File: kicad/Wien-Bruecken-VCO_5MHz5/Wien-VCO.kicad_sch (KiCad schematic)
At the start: 26 parts, among them J1 J113, U1 ${SIM.NAME}, U2 ${SIM.NAME}

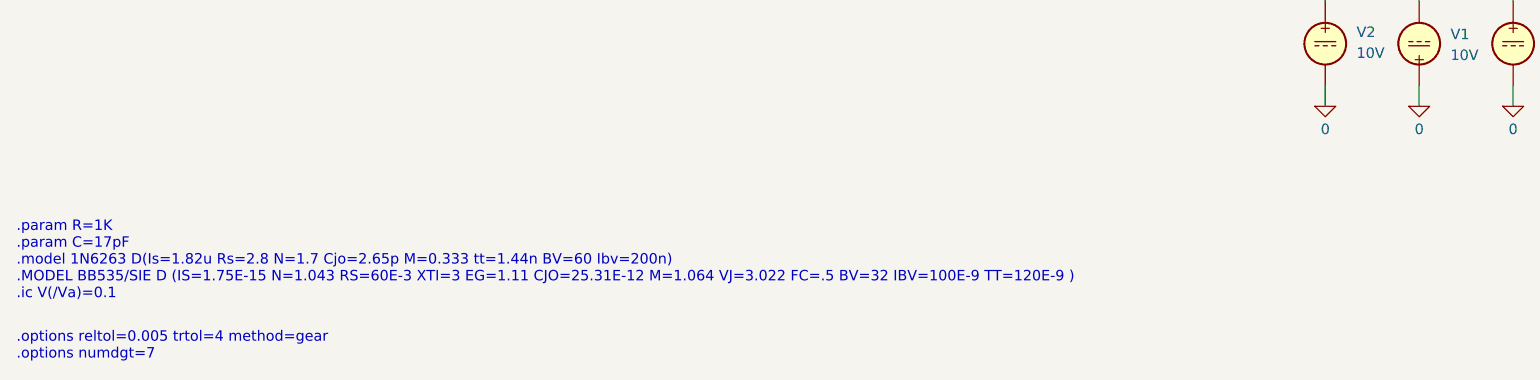
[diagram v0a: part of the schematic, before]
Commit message: sim Ordner angepasst
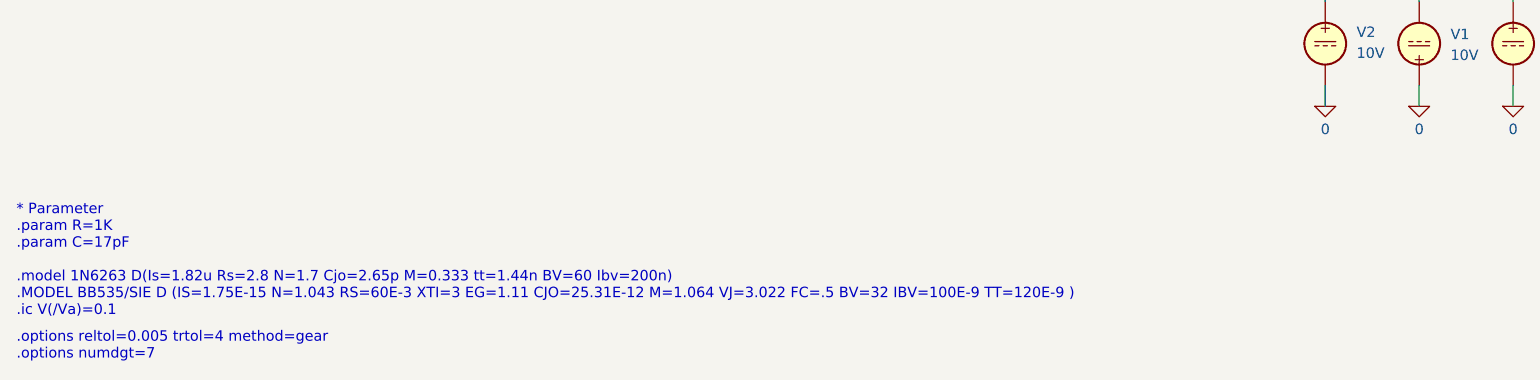
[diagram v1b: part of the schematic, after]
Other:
- note added: "* Parameter .param R=1K .param C=17pF .model 1N6263 D(Is=1.82u Rs=2.8 N=1.7 Cjo=2.65p M=0.333 tt=1.44n BV=60 Ibv=200n) .MODEL BB535/SIE D (IS=1.75E-15 N=1.043 RS=60E-3 XTI=3 EG=1.11 CJO=25.31E-12 M=1.064 VJ=3.022 FC=.5 BV=32 IBV=100E-9 TT=120E-9 ) .ic V(/Va)=0.1"
- note removed: ".param R=1K .param C=17pF .model 1N6263 D(Is=1.82u Rs=2.8 N=1.7 Cjo=2.65p M=0.333 tt=1.44n BV=60 Ibv=200n) .MODEL BB535/SIE D (IS=1.75E-15 N=1.043 RS=60E-3 XTI=3 EG=1.11 CJO=25.31E-12 M=1.064 VJ=3.022 FC=.5 BV=32 IBV=100E-9 TT=120E-9 ) .ic V(/Va)=0.1"
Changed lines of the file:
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@@
 	(generator_version "10.0")
 	(paper "A4")
-	(text ".param R=1K\n.param C=17pF\n.model 1N6263 D(Is=1.82u Rs=2.8 N=1.7 Cjo=2.65p M=0.333 tt=1.44n BV=60 Ibv=200n)\n.MODEL BB535/SIE D (IS=1.75E-15 N=1.043 RS=60E-3 XTI=3 EG=1.11 CJO=25.31E-12 M=1.064 VJ=3.022 FC=.5 BV=32 IBV=100E-9 TT=120E-9 )\n.ic V(/Va)=0.1"
+	(text "* Parameter\n.param R=1K\n.param C=17pF\n\n.model 1N6263 D(Is=1.82u Rs=2.8 N=1.7 Cjo=2.65p M=0.333 tt=1.44n BV=60 Ibv=200n)\n.MODEL BB535/SIE D (IS=1.75E-15 N=1.043 RS=60E-3 XTI=3 EG=1.11 CJO=25.31E-12 M=1.064 VJ=3.022 FC=.5 BV=32 IBV=100E-9 TT=120E-9 )\n.ic V(/Va)=0.1\n"
 		(exclude_from_sim no)
 		(at 19.812 177.546 0)
